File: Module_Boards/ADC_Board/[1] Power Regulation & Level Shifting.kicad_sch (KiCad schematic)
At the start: 26 parts, among them U2 TXB0104RUTR, U3 TPS22916CYFPR, U4 TPS7A9401DSCR

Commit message: Big push. Fixed the issues that were pending. See github
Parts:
- removed C6, C9: 10u0 16V, X-MODs_PcbLib:C0402, symbol X-MODs_SchLib:GRM155R60G106ME01D
- added C6: 22u0 6V3, X-MODs_PcbLib:C0402, symbol X-MODs_SchLib:CL05A226MQ5CUN
- added C9: 10n0 16V, X-MODs_PcbLib:C0402, symbol X-MODs_SchLib:CL05B103JO5NNWC
- C7: value 10u0 16V -> 10n0 16V; symbol X-MODs_SchLib:GRM155R60G106ME01D -> X-MODs_SchLib:CL05B103JO5NNWC; MPN GRM155R60G106ME01D -> CL05B103JO5NNWC
- C8: value 10u0 16V -> 22u0 6V3; symbol X-MODs_SchLib:GRM155R60G106ME01D -> X-MODs_SchLib:CL05A226MQ5CUN; MPN GRM155R60G106ME01D -> CL05A226MQ5CUN
- FB1: value FerriteBead -> 300R; symbol Device:FerriteBead -> X-MODs_SchLib:LI0402B301R-10; MPN (none) -> LI0402B301R-10
- R10, R12: value TBD -> 1R00; symbol X-MODs_SchLib:R -> X-MODs_SchLib:CRCW04021R00FKEDHP; MPN (none) -> CRCW04021R00FKEDHP
- R11, R9: value TBD -> 0R30; symbol X-MODs_SchLib:R -> X-MODs_SchLib:ERJ-2BQJR30X; MPN (none) -> ERJ-2BQJR30X
- R13: now not fitted
- R15: value TBD -> 100K; symbol X-MODs_SchLib:R -> X-MODs_SchLib:CRCW0402100KFKEDC; MPN (none) -> CRCW0402100KFKEDC
- R7: value TBD -> 169K; symbol X-MODs_SchLib:R -> X-MODs_SchLib:CRCW0402169KFKTD; MPN (none) -> CRCW0402169KFKTD
- R8: value TBD -> 1M37; symbol X-MODs_SchLib:R -> X-MODs_SchLib:CRCW04021M37FKED; MPN (none) -> CRCW04021M37FKED
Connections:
- net +3V3: now also FB1.1, C6.1; no longer FB1.2
- net +3V3_FILT: now also FB1.2, C9.1; no longer FB1.1
- net at R12.1: now also C9.2
- net at R9.1: now also C6.2
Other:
- moved on the sheet: C10, C11, C13, C3, C4, C5, C7, C8, FB1, R10, R11, R12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

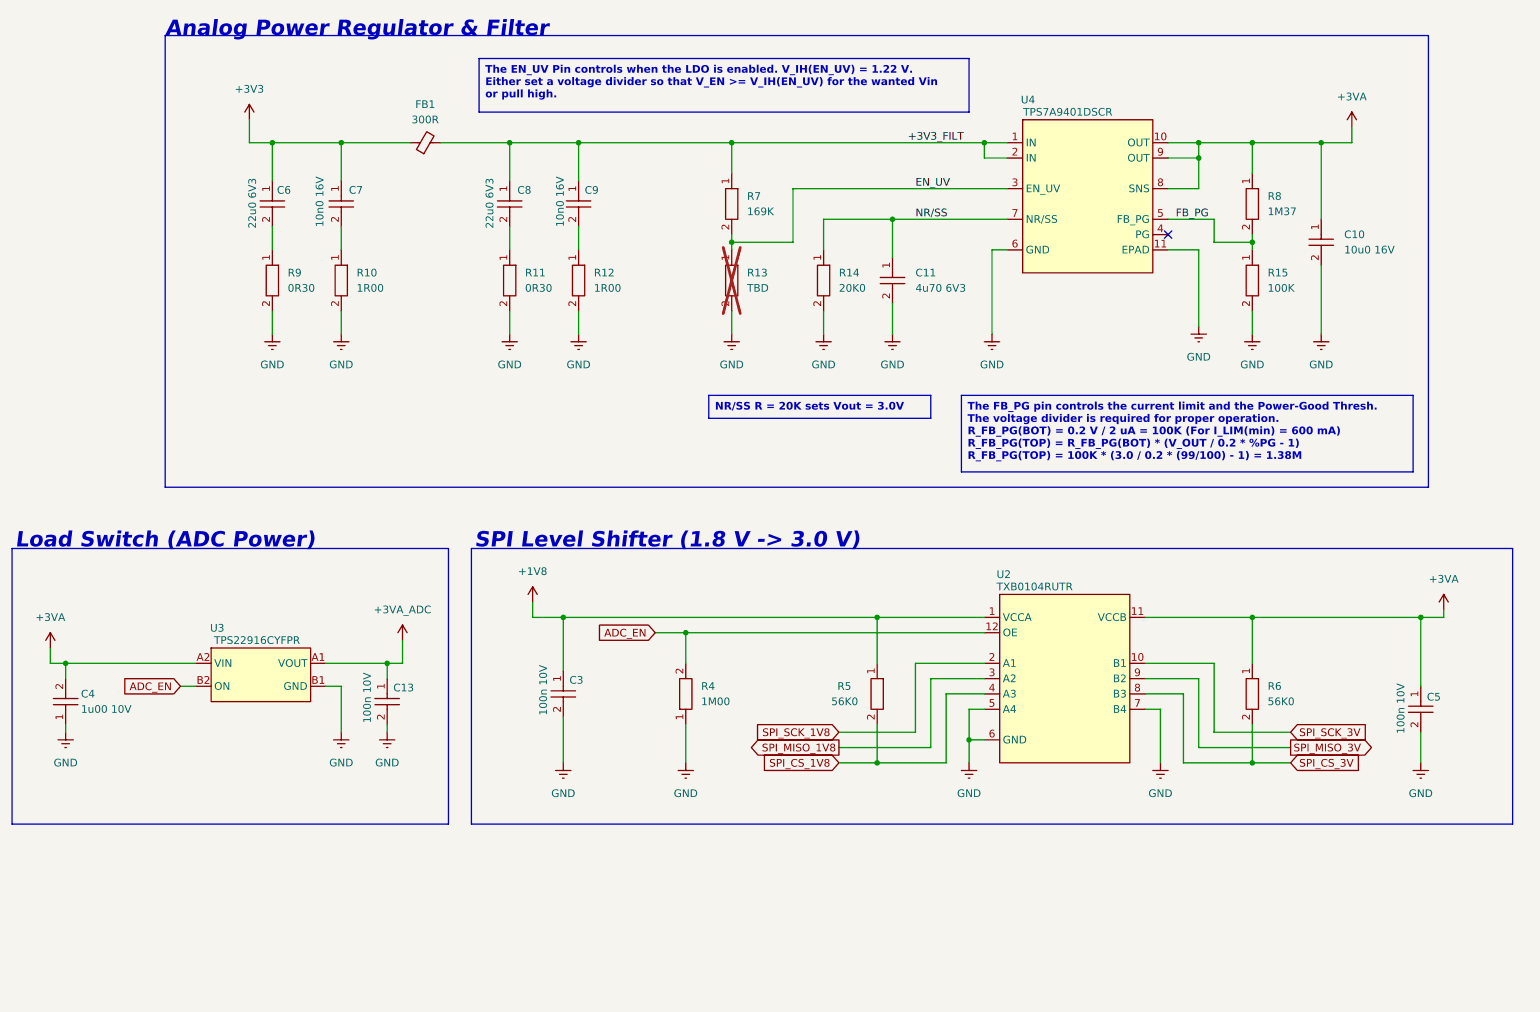
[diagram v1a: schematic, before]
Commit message: Fixed bugs. Added comments. Push before changing the ADC
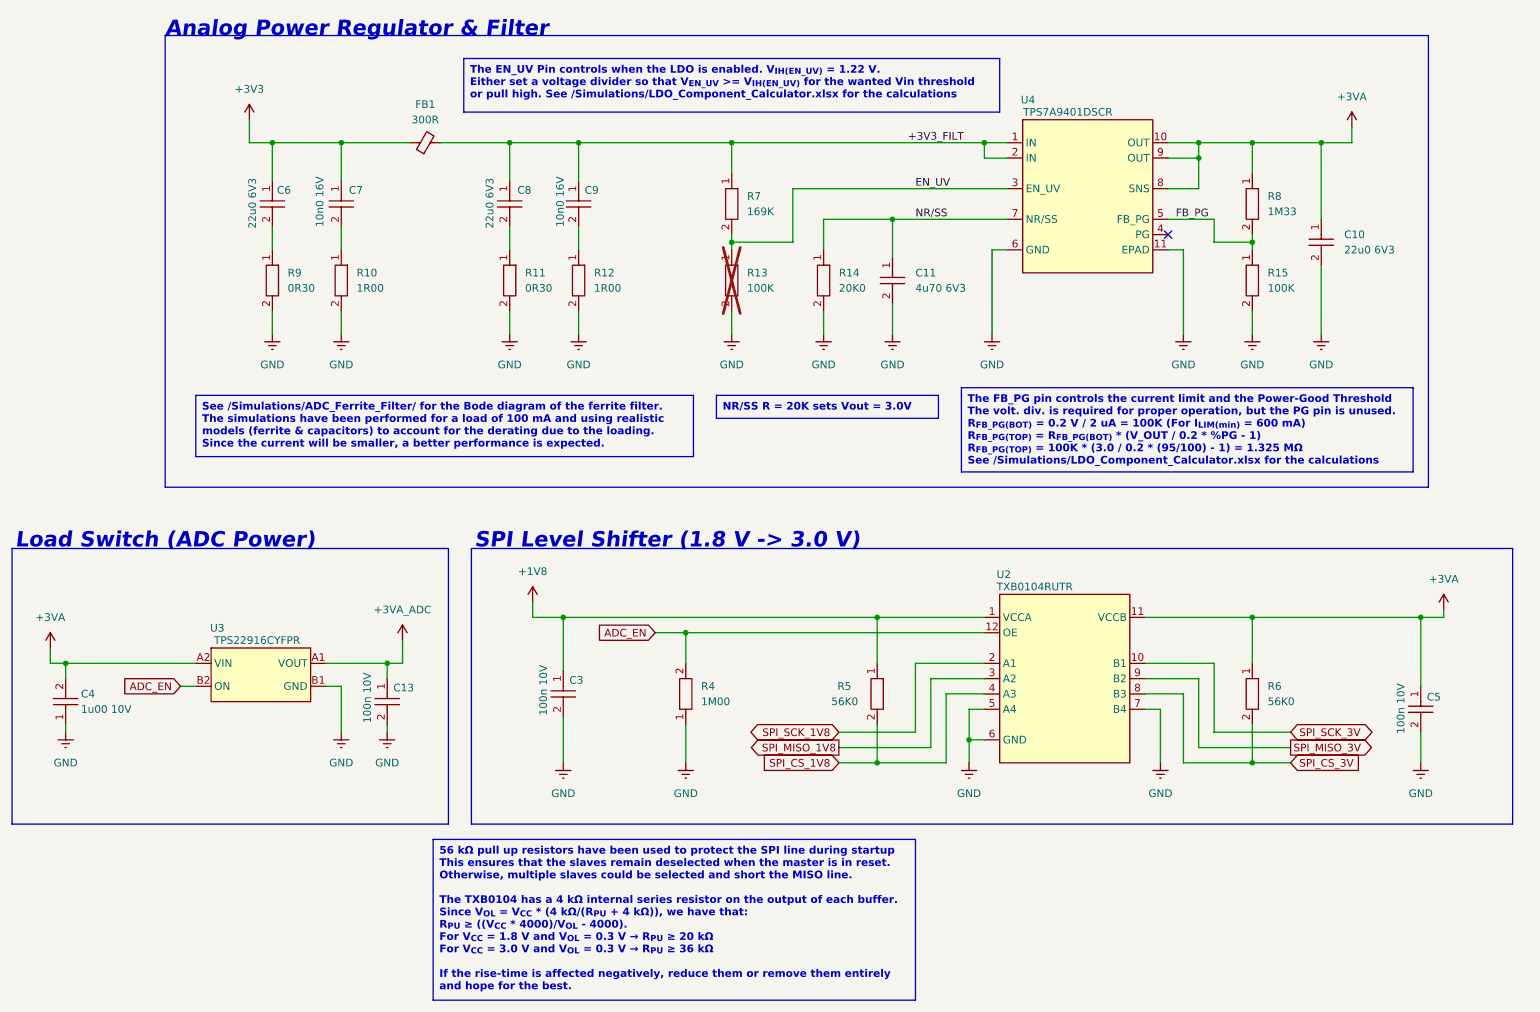
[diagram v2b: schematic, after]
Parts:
- C10: value 10u0 16V -> 22u0 6V3; symbol X-MODs_SchLib:GRM155R60G106ME01D -> X-MODs_SchLib:CL05A226MQ5CUN; MPN GRM155R60G106ME01D -> CL05A226MQ5CUN
- R13: value TBD -> 100K; symbol X-MODs_SchLib:R -> X-MODs_SchLib:CRCW0402100KFKEDC; MPN (none) -> CRCW0402100KFKEDC
- R8: value 1M37 -> 1M33; symbol X-MODs_SchLib:CRCW04021M37FKED -> X-MODs_SchLib:CRCW04021M33FKED; MPN CRCW04021M37FKED -> CRCW04021M33FKED
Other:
- company: (none) -> Embedded Systems Laboratory - EPFL
- title: (none) -> [1] Power Regulation & Level Shifting
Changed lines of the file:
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@@
 	(generator_version "8.0")
 	(paper "A4")
+	(title_block
+		(title "[1] Power Regulation & Level Shifting")
+		(rev "1.0")
+		(company "Embedded Systems Laboratory - EPFL")
+		(comment 1 "Author: José Angel Miranda Calero")
+		(comment 2 "Author: Juan Sapriza")
+		(comment 3 "Author: Alejandro López Rodriguez")
+	)
 	(junction
 		(at 86.36 130.81)
@@
 	(wire
 		(pts
-			(xy 215.9 62.23) (xy 220.98 62.23)
+			(xy 215.9 62.23) (xy 218.44 62.23)
 		)
 		(stroke
@@
 	(wire
 		(pts
-			(xy 220.98 62.23) (xy 220.98 74.93)
+			(xy 218.44 62.23) (xy 218.44 76.2)
 		)
 		(stroke
@@
 		)
 	)
-	(text_box "The FB_PG pin controls the current limit and the Power-Good Thresh. \nThe voltage divider is required for proper operation.\nR_FB_PG(BOT) = 0.2 V / 2 uA = 100K (For I_LIM(min) = 600 mA) \nR_FB_PG(TOP) = R_FB_PG(BOT) * (V_OUT / 0.2 * %PG - 1) \nR_FB_PG(TOP) = 100K * (3.0 / 0.2 * (99/100) - 1) = 1.38M\n "
+	(text_box "The FB_PG pin controls the current limit and the Power-Good Threshold\nThe volt. div. is required for proper operation, but the PG pin is unused.\nR_{FB_PG(BOT)} = 0.2 V / 2 uA = 100K (For I_{LIM(min)} = 600 mA) \nR_{FB_PG(TOP)} = R_{FB_PG(BOT)} * (V_OUT / 0.2 * %PG - 1) \nR_{FB_PG(TOP)} = 100K * (3.0 / 0.2 * (95/100) - 1) = 1.325 MΩ\nSee /Simulations/LDO_Component_Calculator.xlsx for the calculations "
 		(exclude_from_sim no)
-		(at 181.61 86.36 0)
-		(size 74.93 12.7)
+		(at 181.61 85.09 0)
+		(size 74.93 13.97)
 		(stroke
 			(width 0)
@@
 		)
 	)
-	(text_box "The EN_UV Pin controls when the LDO is enabled. V_IH(EN_UV) = 1.22 V.\nEither set a voltage divider so that V_EN >= V_IH(EN_UV) for the wanted Vin\nor pull high."
+	(text_box "The EN_UV Pin controls when the LDO is enabled. V_{IH(EN_UV)} = 1.22 V.\nEither set a voltage divider so that V_{EN_UV} >= V_{IH(EN_UV)} for the wanted Vin threshold\nor pull high. See /Simulations/LDO_Component_Calculator.xlsx for the calculations"
 		(exclude_from_sim no)
-		(at 101.6 30.48 0)
-		(size 81.28 8.89)
+		(at 99.06 30.48 0)
+		(size 88.9 8.89)
 		(stroke
 			(width 0)
@@
 	(text_box "NR/SS R = 20K sets Vout = 3.0V"
 		(exclude_from_sim no)
-		(at 139.7 86.36 0)
+		(at 140.97 86.36 0)
 		(size 36.83 3.81)
 		(stroke
@@
 		)
 	)
+	(text_box "56 kΩ pull up resistors have been used to protect the SPI line during startup \nThis ensures that the slaves remain deselected when the master is in reset. \nOtherwise, multiple slaves could be selected and short the MISO line. \n\nThe TXB0104 has a 4 kΩ internal series resistor on the output of each buffer.\nSince V_{OL} = V_{CC} * (4 kΩ/(R_{PU} + 4 kΩ)), we have that:\nR_{PU} ≥ ((V_{CC} * 4000)/V_{OL} - 4000). \nFor V_{CC} = 1.8 V and V_{OL} = 0.3 V → R_{PU} ≥ 20 kΩ\nFor V_{CC} = 3.0 V and V_{OL} = 0.3 V → R_{PU} ≥ 36 kΩ\n\nIf the rise-time is affected negatively, reduce them or remove them entirely and hope for the best.\n\n"
+		(exclude_from_sim no)
+		(at 93.98 160.02 0)
+		(size 80.01 26.67)
+		(stroke
+			(width 0)
+			(type default)
+		)
+		(fill
+			(type color)
+			(color 255 255 150 1)
+		)
+		(effects
+			(font
+				(size 1.27 1.27)
+				(thickness 0.254)
+				(bold yes)
+				(color 255 2 0 1)
+			)
+			(justify left top)
+		)
+	)
+	(text_box "See /Simulations/ADC_Ferrite_Filter/ for the Bode diagram of the ferrite filter. \nThe simulations have been performed for a load of 100 mA and using realistic \nmodels (ferrite & capacitors) to account for the derating due to the loading. \nSince the current will be smaller, a better performance is expected."
+		(exclude_from_sim no)
+		(at 54.61 86.36 0)
+		(size 82.55 10.16)
+		(stroke
+			(width 0)
+			(type default)
+		)
+		(fill
+			(type color)
+			(color 255 255 150 1)
+		)
+		(effects
+			(font
+				(size 1.27 1.27)
+				(thickness 0.254)
+				(bold yes)
+				(color 255 2 0 1)
+			)
+			(justify left top)
+		)
+	)
 	(text "Load Switch (ADC Power)"
 		(exclude_from_sim no)
@@
 	)
 	(global_label "SPI_SCK_1V8"
-		(shape input)
+		(shape bidirectional)
 		(at 161.29 142.24 180)
 		(fields_autoplaced yes)
@@
 	)
 	(global_label "SPI_SCK_3V"
-		(shape input)
+		(shape bidirectional)
 		(at 236.22 142.24 0)
 		(fields_autoplaced yes)
@@
 	)
 	(symbol
-		(lib_id "X-MODs_SchLib:GRM155R60G106ME01D")
+		(lib_id "X-MODs_SchLib:CL05A226MQ5CUN")
 		(at 241.3 60.96 270)
 		(unit 1)
@@
 			)
 		)
-		(property "Value" "10u0 16V"
+		(property "Value" "22u0 6V3"
 			(at 245.11 62.2299 90)
 			(effects
@@
 		)
 		(property "Footprint" "X-MODs_PcbLib:C0402"
-			(at 233.68 37.084 0)
+			(at 233.68 37.338 0)
 			(effects
 				(font
@@
 			)
 		)
-		(property "Datasheet" "https://www.mouser.es/datasheet/2/281/1/GRM155R60G106ME01_01A-1983785.pdf"
-			(at 235.458 69.596 0)
+		(property "Datasheet" "https://www.mouser.es/datasheet/2/585/Samsung_7_14_2022_CL05A226MQ5QUN_Specsheet-3000115.pdf"
+			(at 235.458 78.486 0)
 			(effects
 				(font
@@
 			)
 		)
-		(property "Description" "Multilayer Ceramic Capacitors MLCC - SMD/SMT 10 uF 4 VDC 20% 0402 X5R"
-			(at 237.236 62.738 0)
+		(property "Description" "Multilayer Ceramic Capacitors MLCC - SMD/SMT 0402, X5R, 22uF, +/-20%"
+			(at 237.236 63.754 0)
 			(effects
 				(font
@@
 			)
 		)
-		(property "MPN" "GRM155R60G106ME01D"
-			(at 231.902 35.56 0)
+		(property "MPN" "CL05A226MQ5CUN"
+			(at 231.902 35.306 0)
 			(effects
 				(font
@@
 	(symbol
 		(lib_id "power:Earth")
-		(at 220.98 74.93 0)
+		(at 218.44 76.2 0)
 		(unit 1)
 		(exclude_from_sim no)
@@
 		(fields_autoplaced yes)
 		(property "Reference" "#PWR019"
-			(at 220.98 81.28 0)
+			(at 218.44 82.55 0)
 			(effects
 				(font
@@
 		)
 		(property "Value" "GND"
-			(at 220.98 80.01 0)
+			(at 218.44 81.28 0)
 			(effects
 				(font
@@
 		)
 		(property "Footprint" ""
-			(at 220.98 74.93 0)
+			(at 218.44 76.2 0)
 			(effects
 				(font
@@
 		)
 		(property "Datasheet" "~"
-			(at 220.98 74.93 0)
+			(at 218.44 76.2 0)
 			(effects
 				(font
@@
 		)
 		(property "Description" "Power symbol creates a global label with name \"Earth\""
-			(at 220.98 74.93 0)
+			(at 218.44 76.2 0)
 			(effects
 				(font
@@
 	)
 	(symbol
-		(lib_id "X-MODs_SchLib:R")
+		(lib_id "X-MODs_SchLib:CRCW0402100KFKEDC")
 		(at 143.51 67.31 270)
 		(unit 1)
@@
 			)
 		)
-		(property "Value" "TBD"
+		(property "Value" "100K"
 			(at 146.05 68.5799 90)
 			(effects
@@
 		)
 		(property "Footprint" "X-MODs_PcbLib:R0402"
-			(at 140.208 67.31 0)
+			(at 139.954 52.324 0)
 			(effects
 				(font
 					(size 1.27 1.27)
 				)
+				(justify left)
 				(hide yes)
 			)
 		)
-		(property "Datasheet" ""
-			(at 137.414 70.358 0)
+		(property "Datasheet" "https://www.vishay.com/doc?28773"
+			(at 136.398 52.324 0)
 			(effects
 				(font
 					(size 1.27 1.27)
 				)
+				(justify left)
 				(hide yes)
 			)
 		)
-		(property "Description" ""
-			(at 139.446 69.088 0)
+		(property "Description" "Thick Film Resistors - SMD 1/16watt 100Kohms 1% Commercial Use"
+			(at 138.176 52.324 0)
 			(effects
 				(font
 					(size 1.27 1.27)
 				)
+				(justify left)
 				(hide yes)
 			)
 		)
-		(property "MPN" ""
-			(at 143.51 67.31 0)
+		(property "MPN" "CRCW0402100KFKEDC"
+			(at 134.62 62.992 0)
 			(effects
 				(font
@@
 	)
 	(symbol
-		(lib_id "X-MODs_SchLib:CRCW04021M37FKED ")
+		(lib_id "X-MODs_SchLib:CRCW04021M33FKED ")
 		(at 229.87 54.61 270)
 		(unit 1)
@@
 			)
 		)
-		(property "Value" "1M37"
+		(property "Value" "1M33"
 			(at 232.41 55.8799 90)
 			(effects
@@
 			)
 		)
-		(property "Description" "Thick Film Resistors - SMD 1/16watt 1.37Mohms 1% 100ppm"
+		(property "Description" "Thick Film Resistors - SMD 1/16watt 1.33Mohms 1% 100ppm"
 			(at 224.536 38.608 0)
 			(effects
@@
 			)
 		)
-		(property "MPN" "CRCW04021M37FKED "
+		(property "MPN" "CRCW04021M33FKED "
 			(at 220.726 49.276 0)
 			(effects

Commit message: Added new version of the ADC Board. Better ADC, precision reference. Similar power consumption
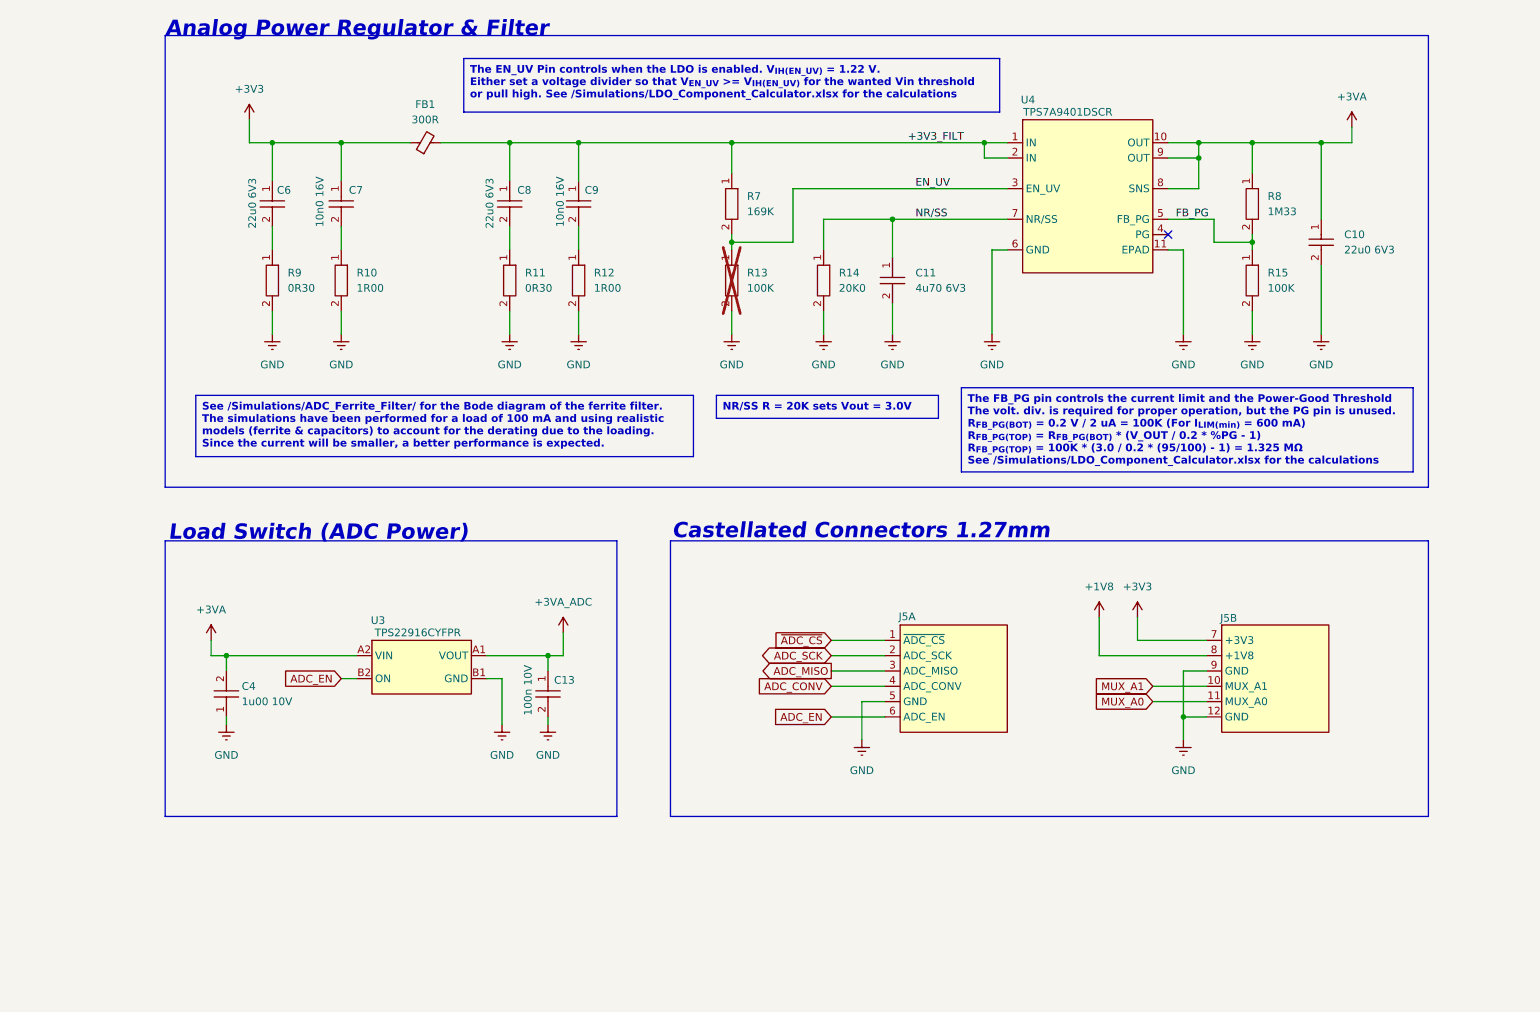
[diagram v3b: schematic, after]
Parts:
- removed C3, C5: 100n 10V, X-MODs_PcbLib:C0402, symbol X-MODs_SchLib:GRM155R71A104JA01D
- removed R4: 1M00, X-MODs_PcbLib:R0402, symbol X-MODs_SchLib:RK73H1ERTTP1004F
- removed R5, R6: 56K0, X-MODs_PcbLib:R0402, symbol X-MODs_SchLib:ERJ-2GEJ563X
- removed U2: TXB0104RUTR, X-MODs_PcbLib:UQFN-12_1.7x2mm, symbol X-MODs_SchLib:TXB0104RUTR
- added J5: ~, X-MODs_PcbLib:ADC_Board_Castellated_Conn_1.27mm, symbol X-MODs_SchLib:ADC_Board_Castellated_Conn_1.27mm
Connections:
- net +1V8: now also J5.8 (+1V8)
- net +3V3: now also J5.7 (+3V3)
- net ADC_EN: now also J5.6 (ADC_EN)
- net GND: now also J5.12 (GND), J5.5 (GND), J5.9 (GND)
- new net ADC_CONV: J5.4 (ADC_CONV)
- new net ADC_MISO: J5.3 (ADC_MISO)
- new net ADC_SCK: J5.2 (ADC_SCK)
- new net MUX_A0: J5.11 (MUX_A0)
- new net MUX_A1: J5.10 (MUX_A1)
- new net ~{ADC_CS}: J5.1 (~{ADC_CS})
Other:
- note added: "Castellated Connectors 1.27mm"
- note removed: "SPI Level Shifter (1.8 V -> 3.0 V)"
- moved on the sheet: C13, C4, U3
